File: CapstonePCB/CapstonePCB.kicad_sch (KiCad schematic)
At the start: 44 parts, among them J1 Conn_02x40_Counter_Clockwise, J2 Barrel_Jack, J3 512964594, SW1 SW_Push, SW2 SW_Push, SW3 SW_Push, U1 NUCLEO64-F411RE, U2 LP-MSPM0G3507, U3 STSPIN220, U4 SN74AHC14N, U5 LM7805_TO220, U6 TLV1117-33, U7 COM-09032, U8 APDS-9306, U9 AL5809-20QP1-7

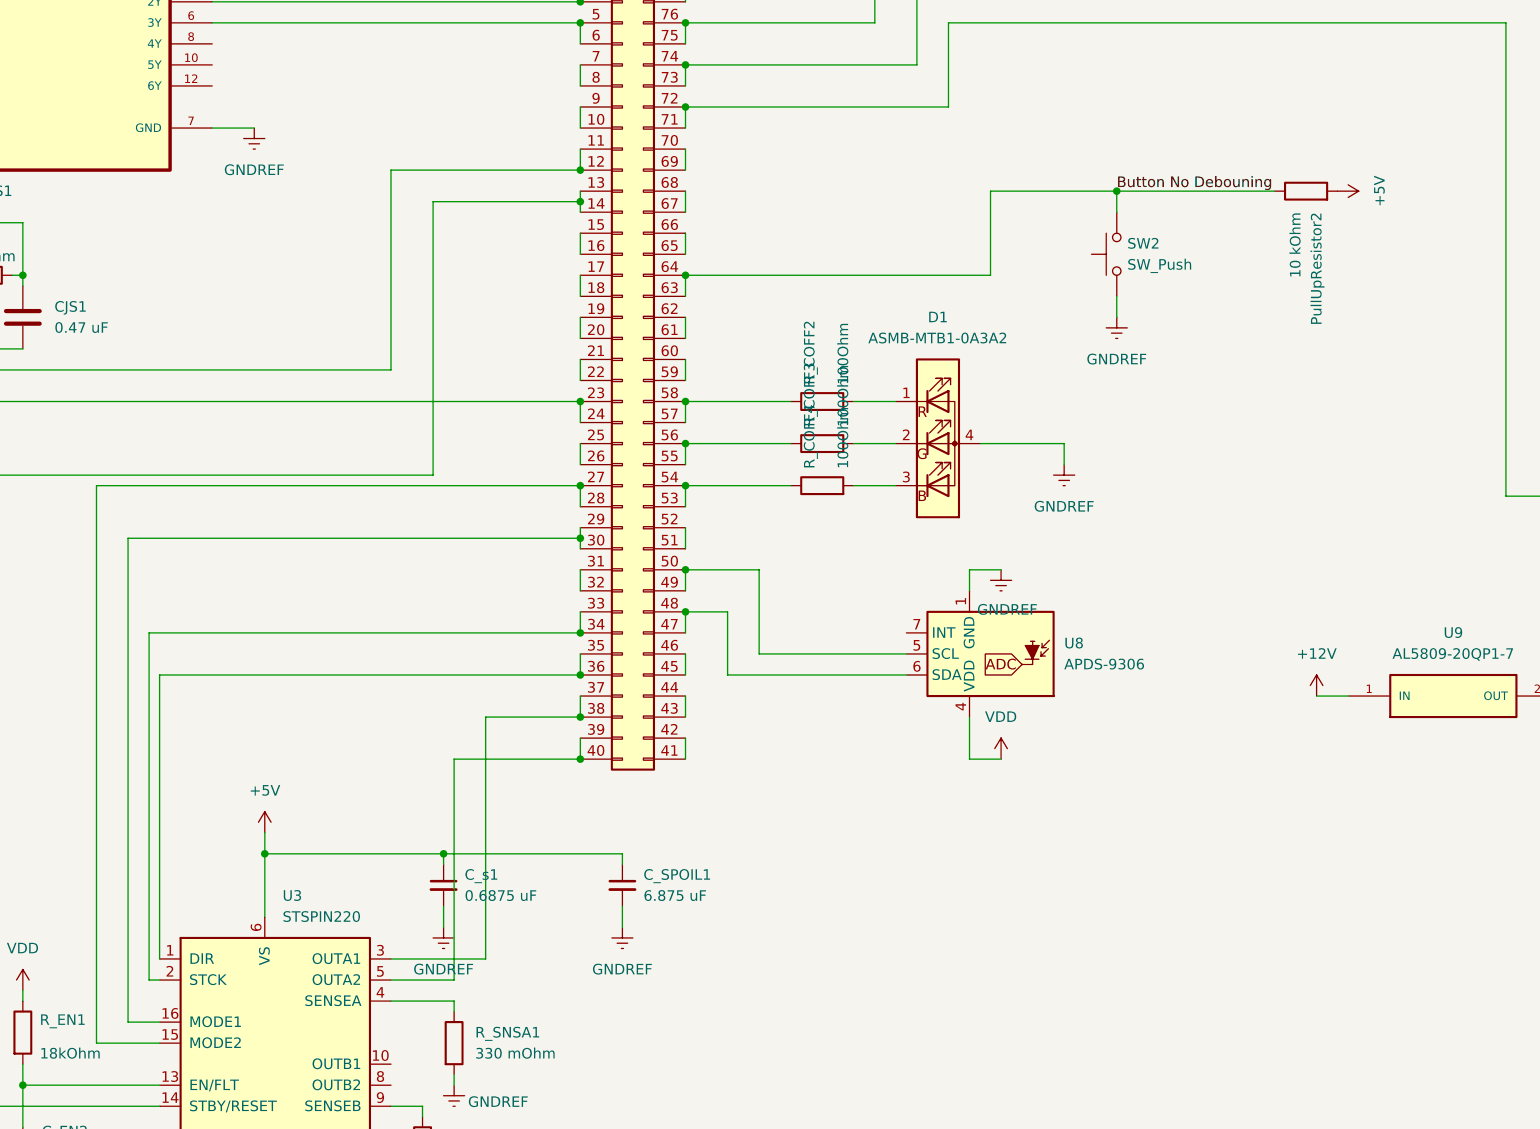
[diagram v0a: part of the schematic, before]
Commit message: Completed routing for PCB
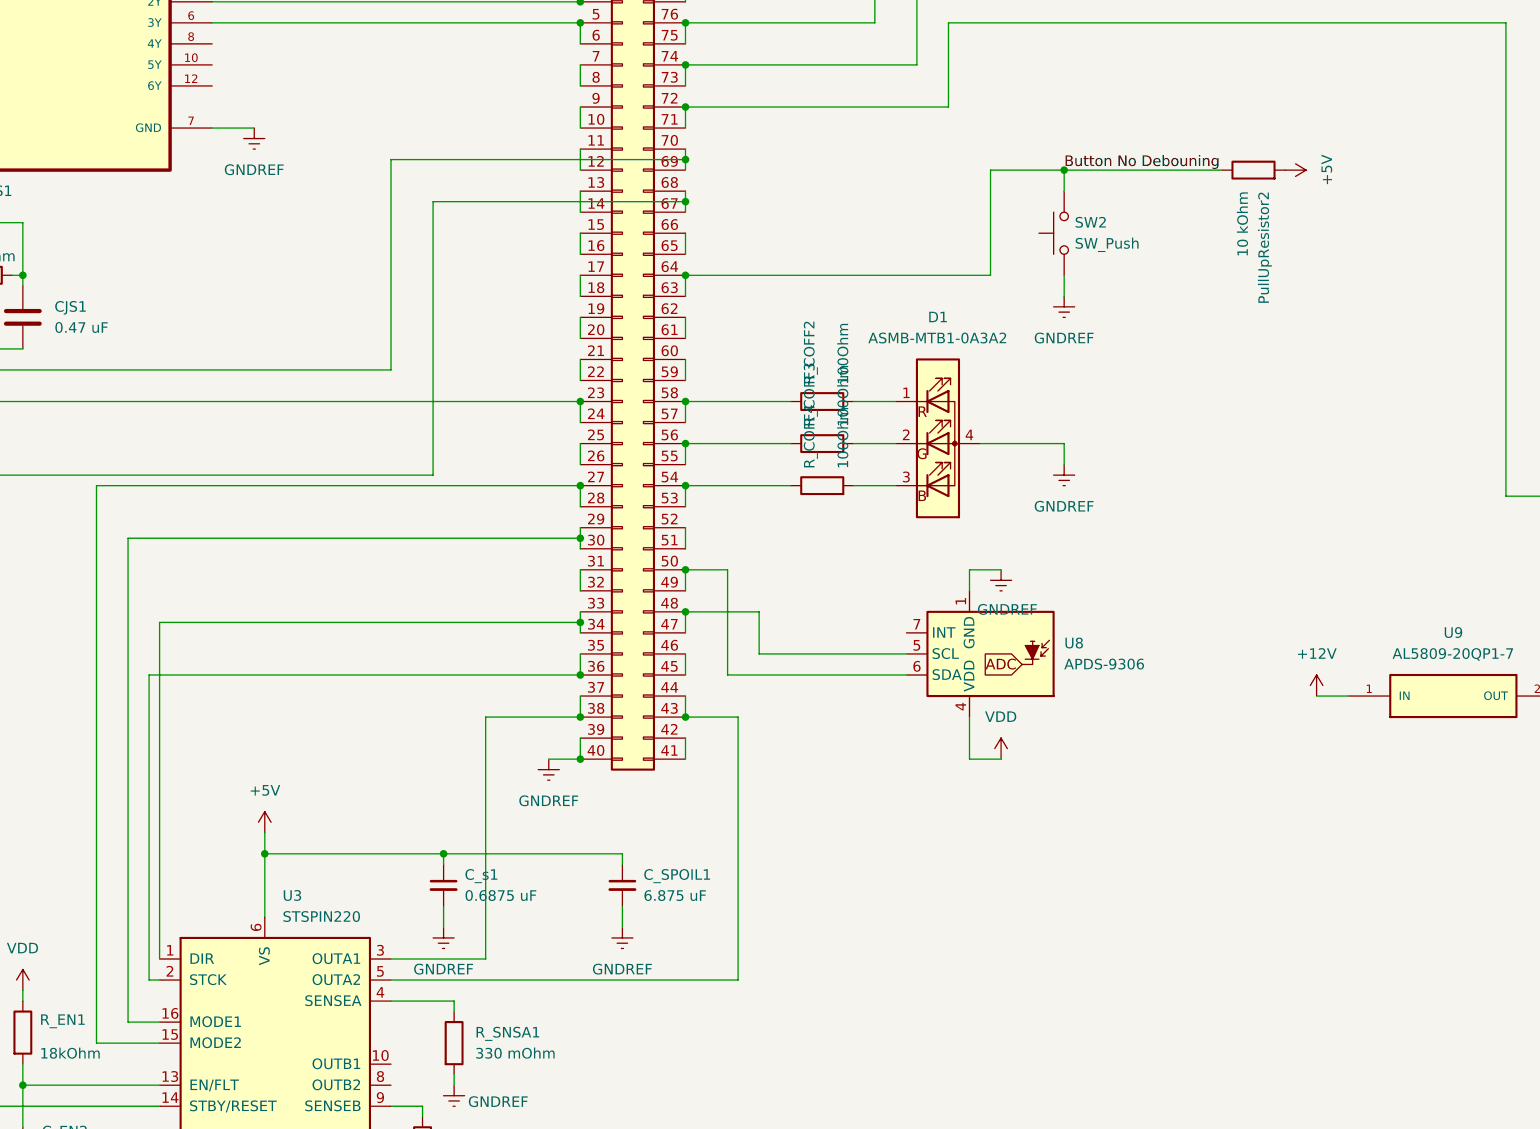
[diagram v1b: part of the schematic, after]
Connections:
- net GNDREF: now also J1.39 (Pin_39), J1.40 (Pin_40)
- net at J1.49 (Pin_49), J1.50 (Pin_50): now also U8.6 (SDA); no longer U8.5 (SCL)
- net at J1.47 (Pin_47), J1.48 (Pin_48): now also U8.5 (SCL); no longer U8.6 (SDA)
- net at J1.35 (Pin_35), J1.36 (Pin_36): now also U3.2 (STCK); no longer U3.1 (DIR)
- net at J1.33 (Pin_33), J1.34 (Pin_34): now also U3.1 (DIR); no longer U3.2 (STCK)
- net at J1.11 (Pin_11), J1.12 (Pin_12): no longer U7.H2 (H)
- net at J1.13 (Pin_13), J1.14 (Pin_14): no longer U7.V2 (V)
- net at J1.43 (Pin_43), J1.44 (Pin_44): now also U3.5 (OUTA2)
- net at J1.67 (Pin_67), J1.68 (Pin_68): now also U7.V2 (V)
- net at J1.69 (Pin_69), J1.70 (Pin_70): now also U7.H2 (H)
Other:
- moved on the sheet: PullUpResistor2, SW2

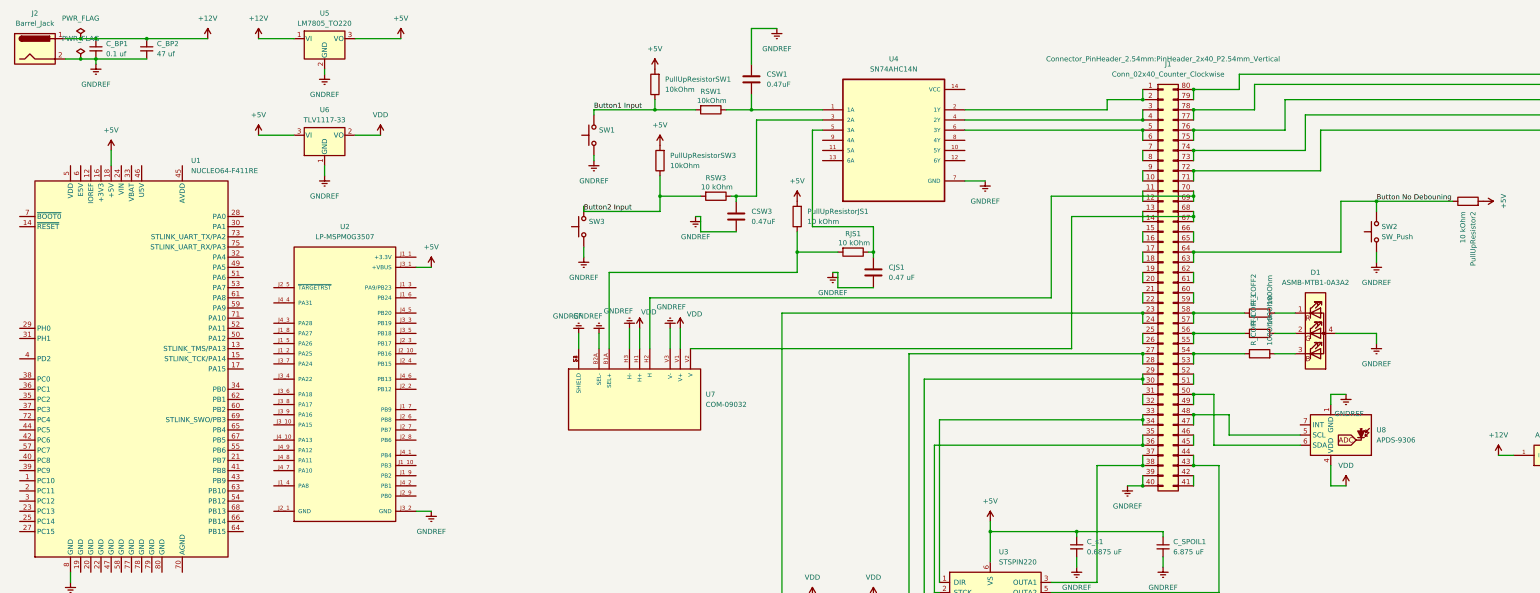
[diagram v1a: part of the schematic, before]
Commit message: Changed I2C light sensor to different type so pin spacing is not an issue
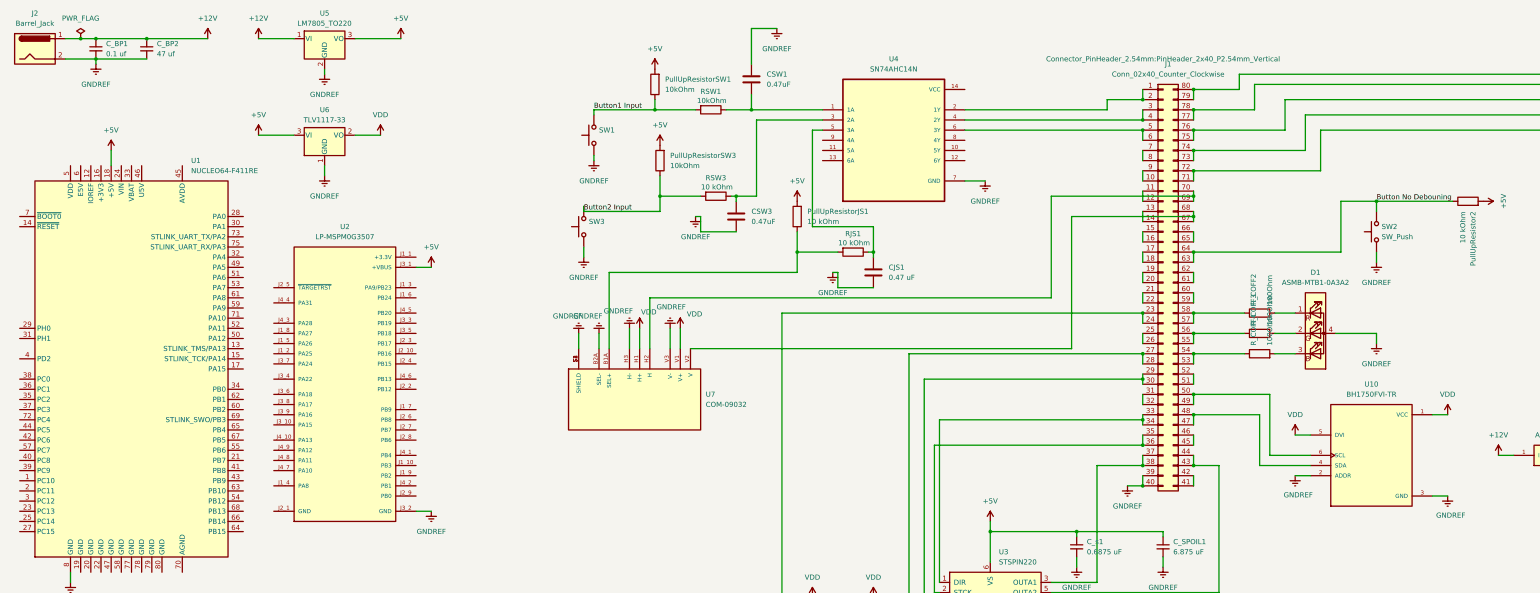
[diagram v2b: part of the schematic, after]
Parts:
- removed U8: APDS-9306, OptoDevice:Broadcom_LGA-8_2x2mm_P0.53mm, symbol Sensor_Optical:APDS-9306
- added U10: BH1750FVI-TR, BH1750FVI-TR:XDCR_BH1750FVI-TR, symbol BH1750FVI-TR:BH1750FVI-TR
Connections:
- net GNDREF: now also U10.2 (ADDR), U10.3 (GND)
- net VDD: now also U10.1 (VCC), U10.5 (DVI)
- net at J1.47 (Pin_47), J1.48 (Pin_48): now also U10.4 (SDA)
- net at J1.49 (Pin_49), J1.50 (Pin_50): now also U10.6 (SCL)

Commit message: Added backlight power for LCD
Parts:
- U9: footprint AL5809-20QP1-7:SODFL3717X100N -> AL5809-20.step:SODFL3717X100N
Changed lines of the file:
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@@
 			)
 		)
-		(property "Footprint" "AL5809-20QP1-7:SODFL3717X100N"
+		(property "Footprint" "AL5809-20.step:SODFL3717X100N"
 			(at 406.4 124.46 0)
 			(effects

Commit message: Changed buttons to use 3.3V logic
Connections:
- net +5V: no longer PullUpResistor2.2, PullUpResistorJS1.2, PullUpResistorSW1.2, PullUpResistorSW3.2
- net VDD: now also PullUpResistor2.2, PullUpResistorJS1.2, PullUpResistorSW1.2, PullUpResistorSW3.2

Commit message: Added the buzzer driver
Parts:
- added Q1: 2N7000, Package_TO_SOT_THT:TO-92_Inline, symbol Transistor_FET:2N7000
- added R_BUZ: 100R, Resistor_SMD:R_0201_0603Metric, symbol Device:R
- added R_BUZ2: 100kR, Resistor_SMD:R_0201_0603Metric, symbol Device:R
- added U8: WST-1205S, WST-1205S.step:WST-1205S, symbol WST-1205S:WST-1205S
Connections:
- net +5V: now also Q1.3 (D)
- net GNDREF: now also R_BUZ2.2, U8.-
- net BuzzerGPIO: now reaches J1.65 (Pin_65), J1.66 (Pin_66)
- net BuzzerGPIO: now also R_BUZ.1
- new net: Q1.2 (G), R_BUZ.2, R_BUZ2.1
- new net: Q1.1 (S), U8.+

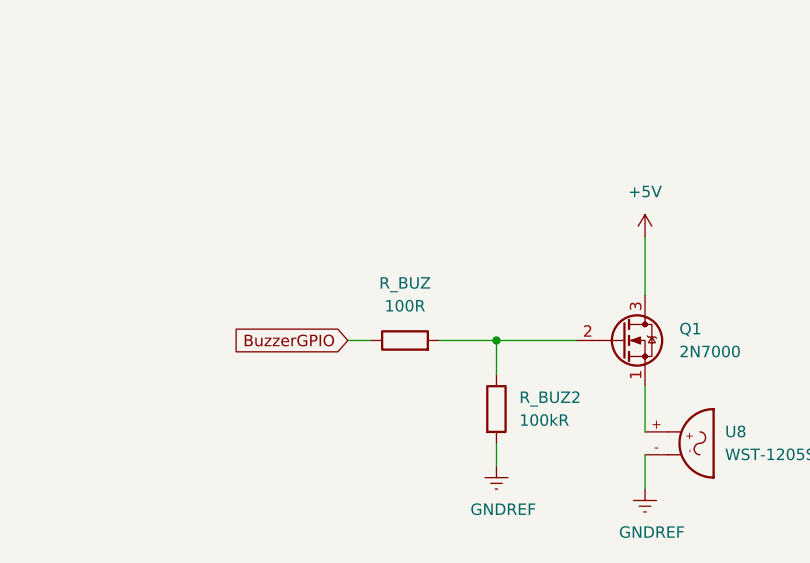
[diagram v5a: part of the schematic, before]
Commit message: Corrected edge cuts layer
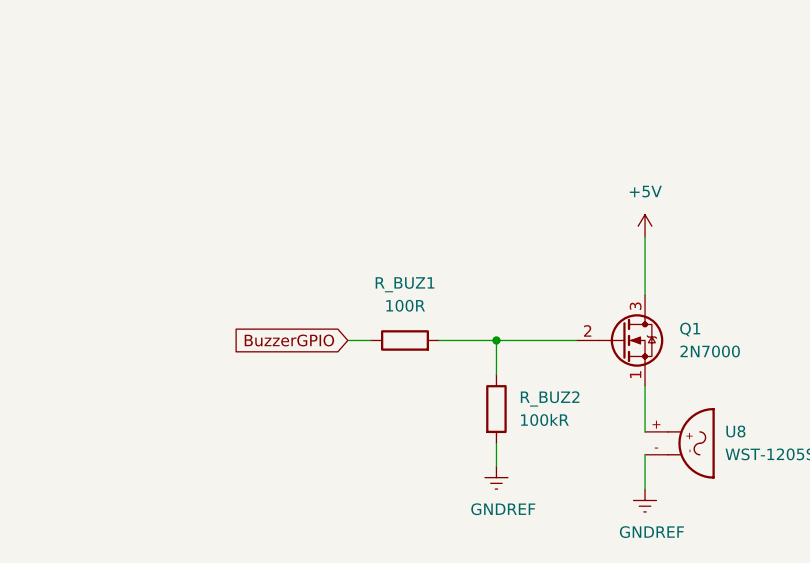
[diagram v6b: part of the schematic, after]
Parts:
- renumbered R_BUZ to R_BUZ1
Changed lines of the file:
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@@
 	(generator "eeschema")
 	(generator_version "9.0")
-	(paper "User" 470 297)
+	(paper "A4")
 	(junction
 		(at 35.56 20.32)
@@
 		(dnp no)
 		(fields_autoplaced yes)
-		(property "Reference" "R_BUZ"
+		(property "Reference" "R_BUZ1"
 			(at 340.36 205.74 90)
 			(effects
@@
 			(project "CapstonePCB"
 				(path "/39e7582f-7765-4fc9-b934-76d5b28d9065"
-					(reference "R_BUZ")
+					(reference "R_BUZ1")
 					(unit 1)
 				)

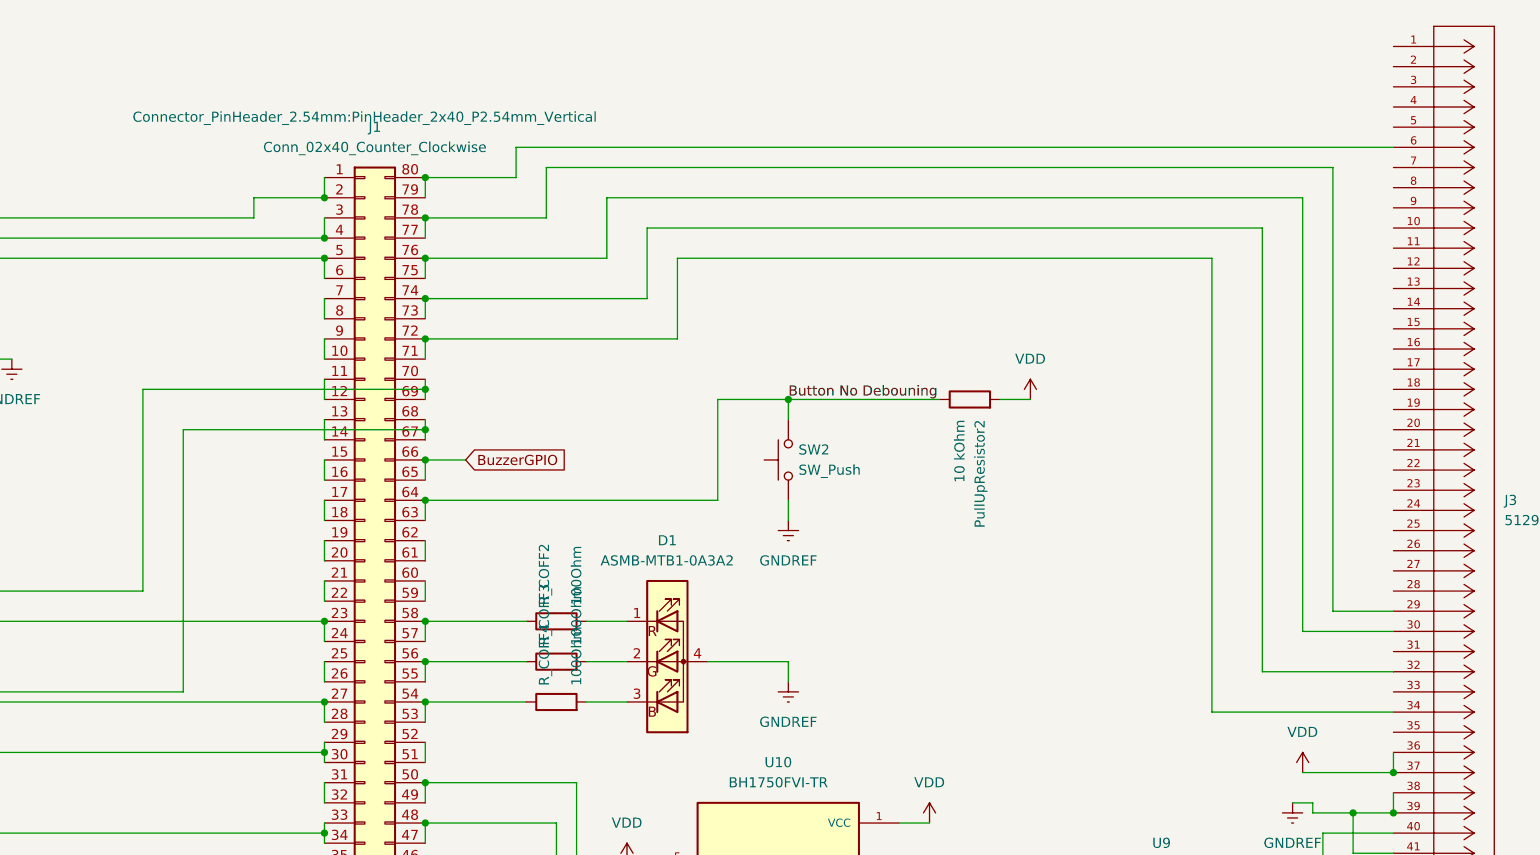
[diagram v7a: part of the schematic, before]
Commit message: Corrected wiring for display for 4 SPI wire
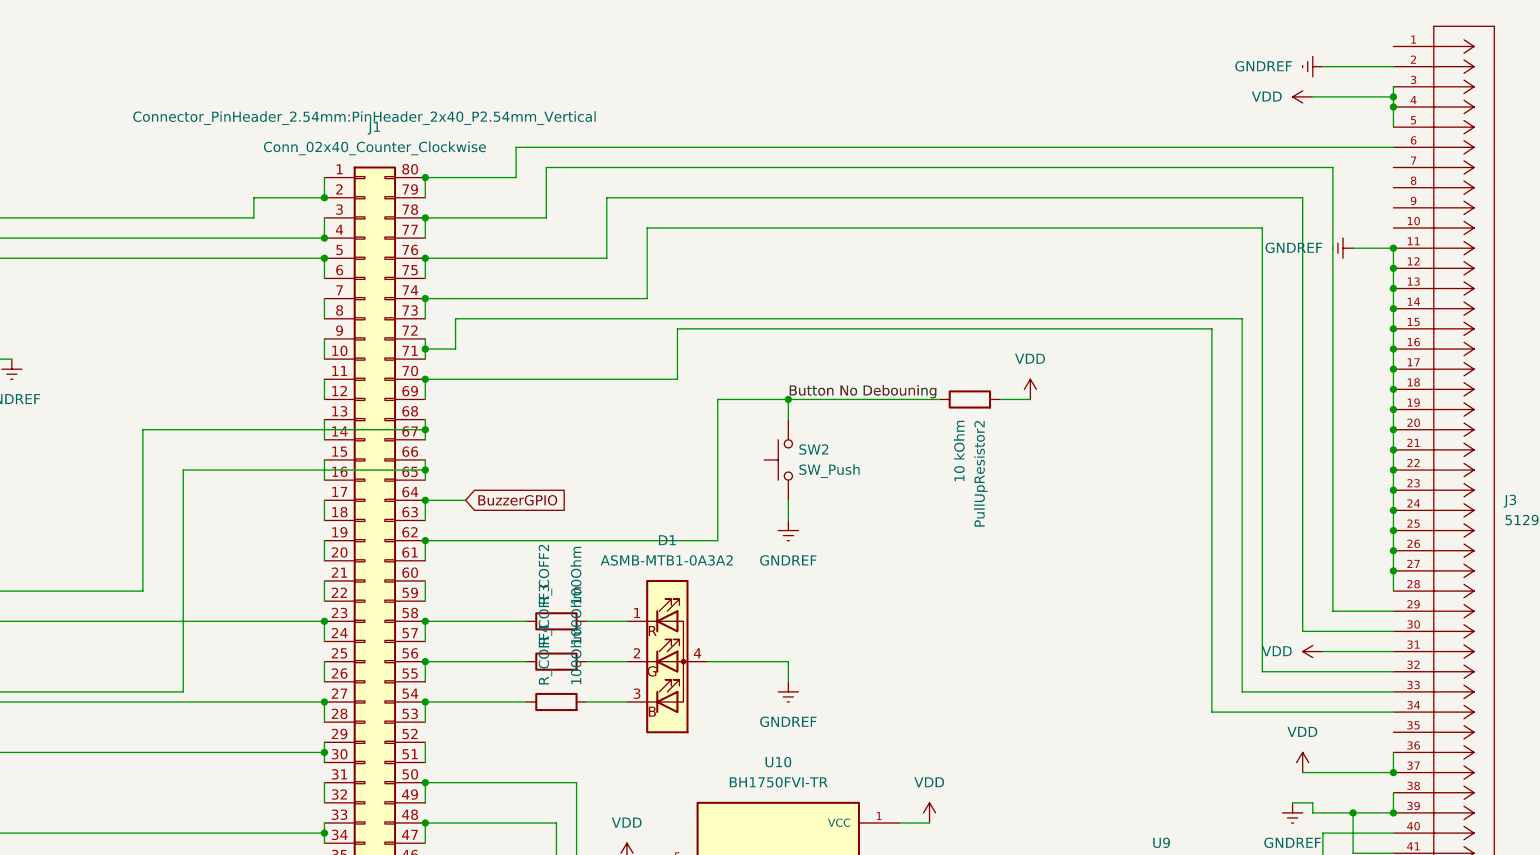
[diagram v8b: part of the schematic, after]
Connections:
- net Button No Debouning: now also J1.61 (Pin_61), J1.62 (Pin_62); no longer J1.63 (Pin_63), J1.64 (Pin_64)
- net BuzzerGPIO: now also J1.63 (Pin_63), J1.64 (Pin_64); no longer J1.65 (Pin_65), J1.66 (Pin_66)
- net GNDREF: now also J3.11, J3.12, J3.13, J3.14, J3.15, J3.16, J3.17, J3.18, J3.19, J3.2, J3.20, J3.21, J3.22, J3.23, J3.24, J3.25, J3.26, J3.27, J3.28
- net VDD: now also J3.3, J3.31, J3.4, J3.5
- net at J1.69 (Pin_69), J1.70 (Pin_70): now also J3.34; no longer U7.H2 (H)
- net at J1.67 (Pin_67), J1.68 (Pin_68): now also U7.H2 (H); no longer U7.V2 (V)
- net at J3.33: now also J1.71 (Pin_71), J1.72 (Pin_72)
- new net: J1.65 (Pin_65), J1.66 (Pin_66), U7.V2 (V)
